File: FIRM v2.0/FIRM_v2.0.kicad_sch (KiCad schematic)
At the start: 131 parts, among them J2 Conn_01x02_Pin, J3 Screw_Terminal_01x04, Q1 IRLML6402, U11 SAM-M10Q, U12 STM32F446ZCHx, U13 SCH16T-K01-10, U5 INA219AxDCN, U9 A-USBC-20F0-EA-GSR05, Y2 12 MHz

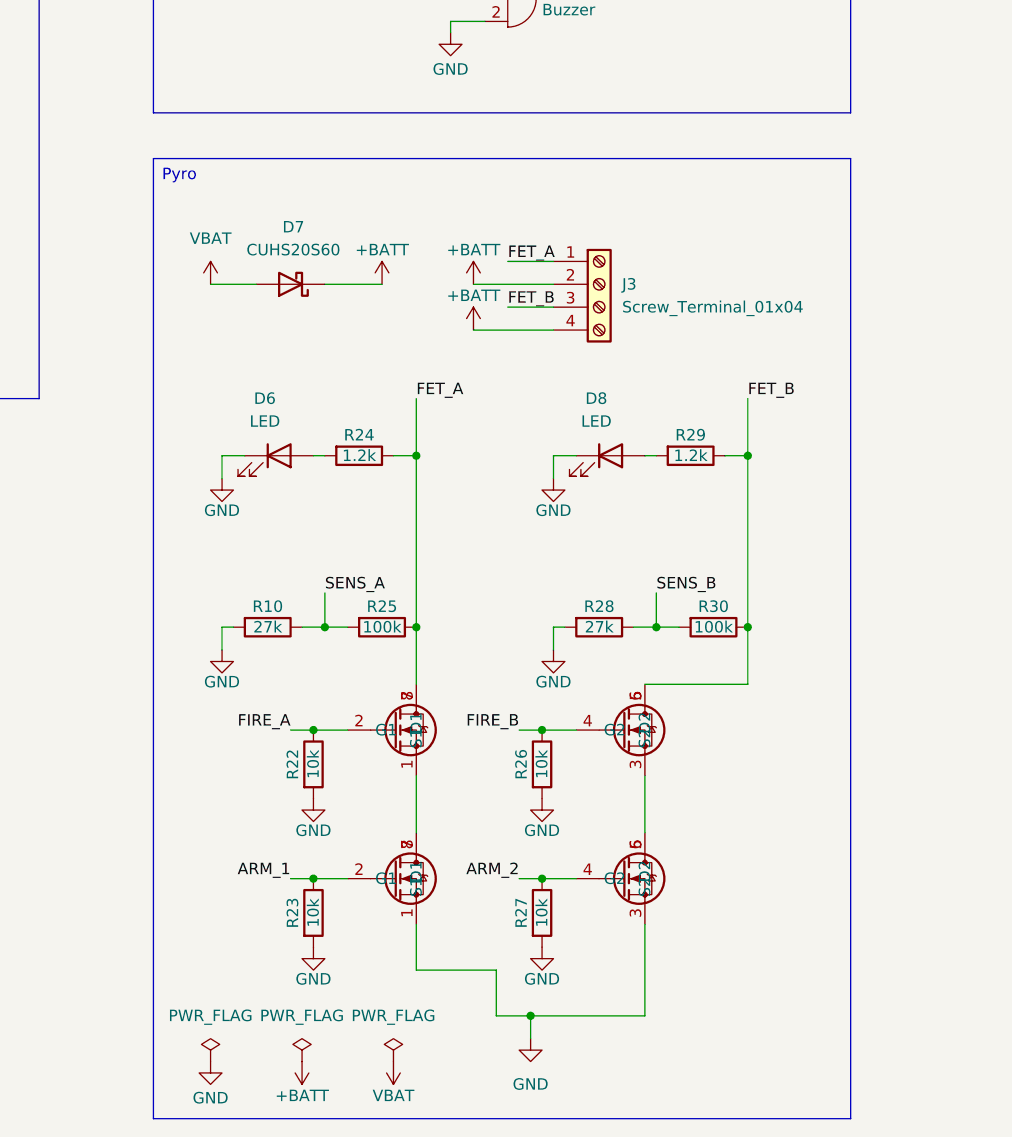
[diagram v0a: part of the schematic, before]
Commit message: Fix Pryo Channels
Replaced TSM200N03D with G120N02D32 because the former didn't have a defined on resistance at a gate voltage of 3.3v. The resistance of G120N02D32 is ~10mOhm at 3.3v V_GS. The mosfet also meets our other requirements of >15v max V_DS & >5mJ max pulse avalanche energy & >15A max pulsed drain current.

Added 220 ohm gate resistors to the mosfets as well to reduce noise and current draw.
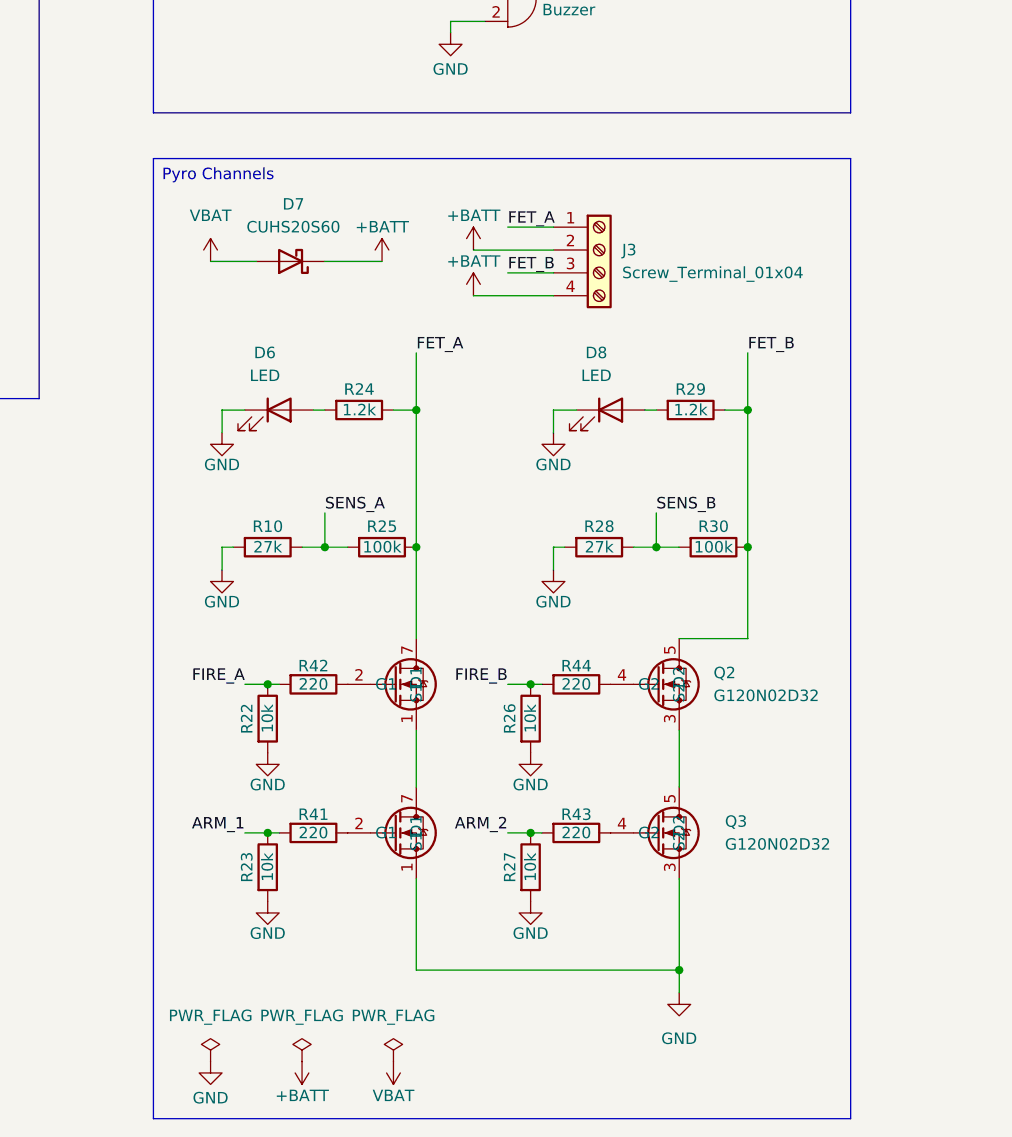
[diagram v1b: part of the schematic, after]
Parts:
- removed M1, M3: (no value), transistors:TSM200N03D, symbol transistors:TSM200N03D
- added Q2, Q3: G120N02D32, HPRC_Transistors:G120N02D32, symbol HPRC_Transistors:G120N02D32
- added R41, R42, R43, R44: 220, symbol Device:R
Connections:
- net ARM_1: now also R41.2
- net ARM_2: now also R43.2
- net FET_A: now also Q2.7 (D1), Q2.8 (D1)
- net FET_B: now also Q2.5 (D2), Q2.6 (D2)
- net FIRE_A: now also R42.2
- net FIRE_B: now also R44.2
- net GND: now also Q3.1 (S1), Q3.3 (S2)
- new net: Q3.4 (G2), R43.1
- new net: Q2.1 (S1), Q3.7 (D1), Q3.8 (D1)
- new net: Q2.2 (G1), R42.1
- new net: Q2.3 (S2), Q3.5 (D2), Q3.6 (D2)
- new net: Q2.4 (G2), R44.1
- new net: Q3.2 (G1), R41.1
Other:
- moved on the sheet: D6, D7, D8, J3, R10, R22, R23, R24, R25, R26, R27, R28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

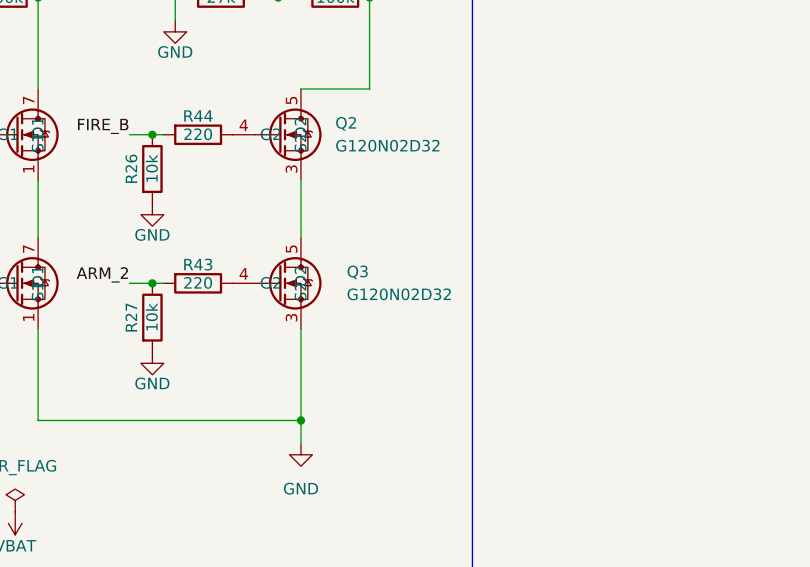
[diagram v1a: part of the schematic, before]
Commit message: Add Resistor Footprints
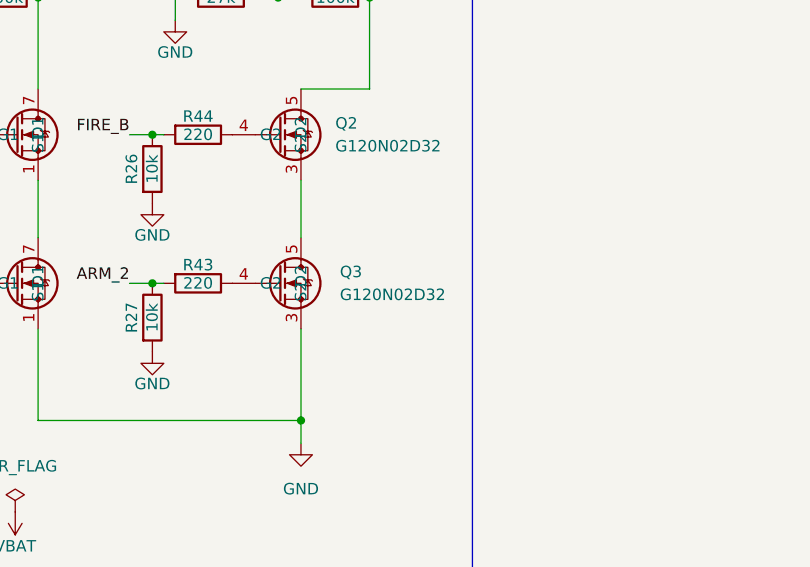
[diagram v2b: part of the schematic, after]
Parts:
- R41, R42, R43, R44: footprint (none) -> Resistor_SMD:R_0402_1005Metric
